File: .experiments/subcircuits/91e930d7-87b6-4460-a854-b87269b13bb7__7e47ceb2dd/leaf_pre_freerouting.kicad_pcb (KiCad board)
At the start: 2 copper layers, 34.9 x 18.6 mm, 13 parts, among them U2 BQ24072

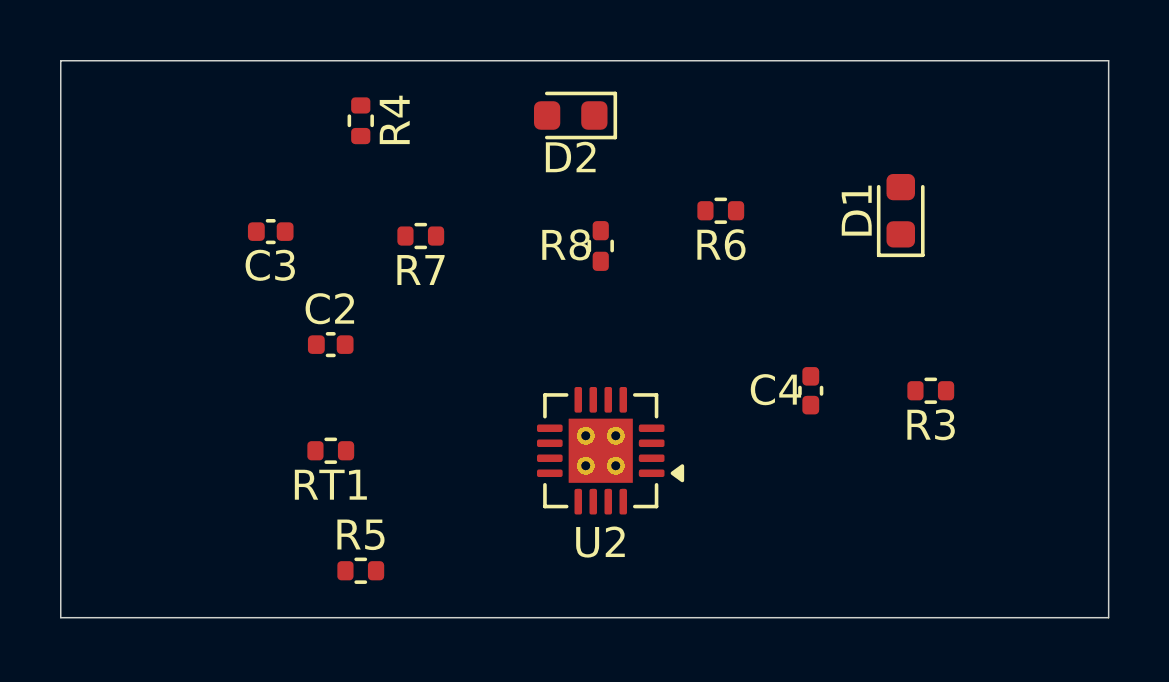
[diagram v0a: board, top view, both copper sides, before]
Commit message: feat: parent board stamping with preserved child copper
- Add --pcb, --stamp, --route, --jar flags to compose_subcircuits.py
- Implement subprocess-based parent board stamping (no pcbnew in main process)
- Add _stamp_parent_board() that copies base PCB, moves footprints to
  composed positions, clears existing tracks/zones, recreates child copper
  traces and vias with proper net name resolution
- Add _route_parent_board() for FreeRouting with preserve_existing_copper
- Add _persist_parent_artifact() for parent solved_layout.json persistence
- Store ParentComposition on ParentCompositionState for downstream access
- Update leaf artifacts from fresh pipeline run (6/6 leaves routed)
- Parent stamp verified: 37 components, 286 child traces, 10 vias preserved
  on real .kicad_pcb board with correct positions and net assignments
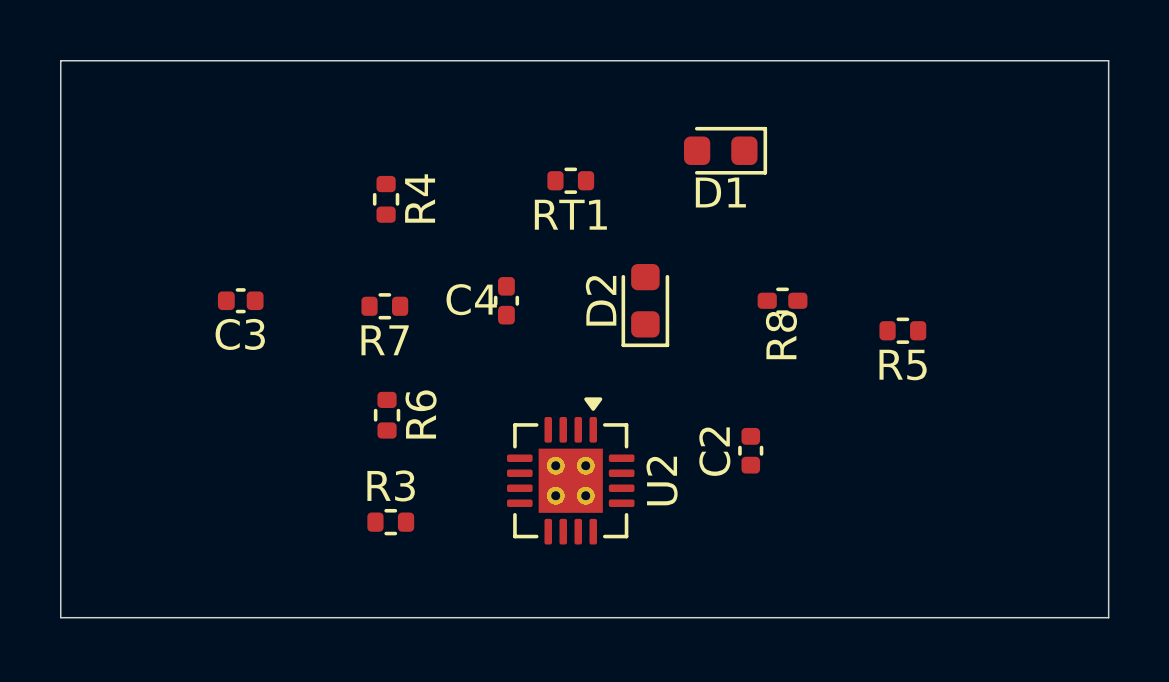
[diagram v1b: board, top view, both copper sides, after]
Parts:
- moved R5 19.8 mm to (28.1, 9.00), turned to 180 degrees
- moved R3 18.5 mm to (11.0, 15.4), turned to 0 degrees
- moved C2 14.4 mm to (23.0, 13.0), turned to 90 degrees
- moved R6 13.0 mm to (10.9, 11.8), turned to -90 degrees
- moved RT1 12.0 mm to (17.0, 4.00)
- moved C4 10.6 mm to (14.9, 8.00)
- moved D2 6.66 mm to (19.5, 8.00), turned to 90 degrees
- moved R8 6.33 mm to (24.1, 8.00), turned to 180 degrees
- moved D1 6.32 mm to (22.0, 3.00), turned to 180 degrees
- moved R4 2.75 mm to (10.8, 4.62)
- moved R7 2.63 mm to (10.8, 8.18)
- moved C3 2.51 mm to (6.00, 8.00)
- moved U2 1.41 mm to (17.0, 14.0), turned to -90 degrees

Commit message: feat: unified hierarchical solver (solve_hierarchy.py)
Single-command entry point for the full subcircuit pipeline:
  python3 solve_hierarchy.py LLUPS.kicad_sch --pcb LLUPS.kicad_pcb --route

Phase 1: Solve leaf subcircuits (delegates to solve_subcircuits.py)
  - 6 leaves solved and routed via FreeRouting
  - Canonical copper persisted in solved_layout.json

Phase 2: Compose and route parent (delegates to compose_subcircuits.py)
  - Grid layout of 6 children with 5mm spacing
  - Child copper preserved on stamped parent board
  - FreeRouting routes interconnect nets between subcircuits
  - Parent artifact persisted with full copper

Flags: --skip-leaves, --leaf-only, --rounds, --mode, --spacing-mm, --jar
Full pipeline completes in ~4 minutes (with routing)
Skip-leaves mode completes in ~28 seconds
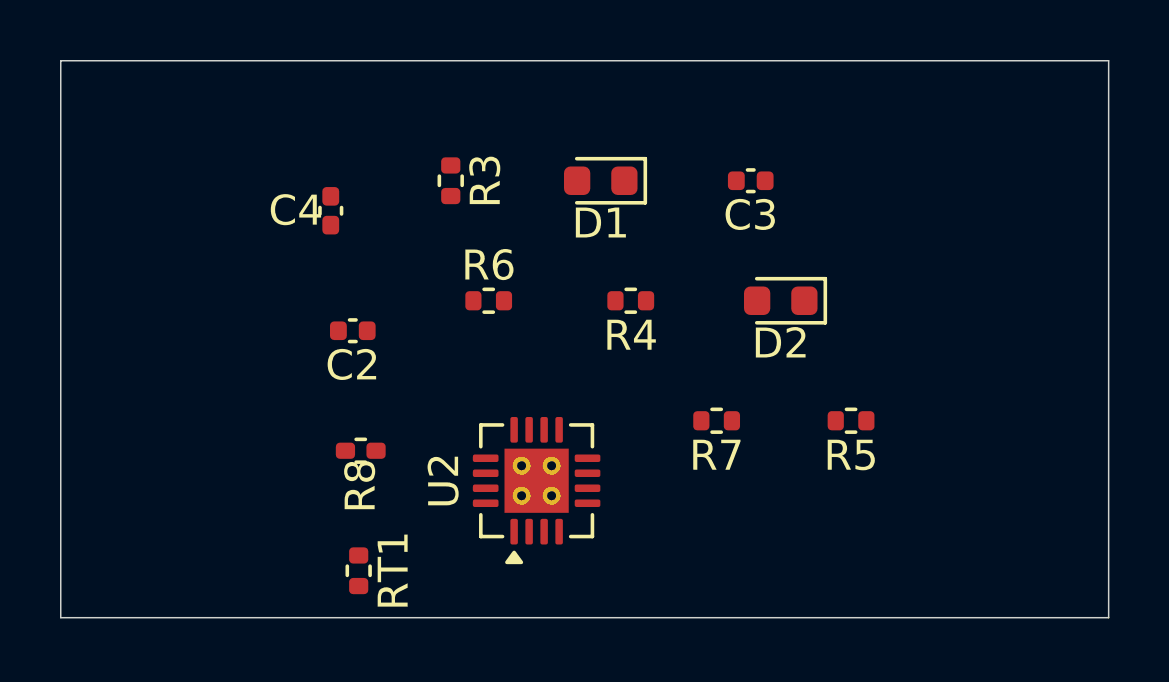
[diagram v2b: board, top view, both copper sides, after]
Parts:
- moved C3 17.5 mm to (23.0, 4.00)
- moved R8 14.9 mm to (10.0, 13.0)
- moved RT1 14.8 mm to (9.93, 17.0), turned to -90 degrees
- moved C2 13.9 mm to (9.73, 9.00), turned to 180 degrees
- moved R7 11.7 mm to (21.9, 12.0)
- moved R3 11.6 mm to (13.0, 4.00), turned to -90 degrees
- moved R4 8.83 mm to (19.0, 8.00), turned to 180 degrees
- moved C4 6.58 mm to (9.00, 5.00)
- moved R6 5.10 mm to (14.3, 8.00), turned to 0 degrees
- moved D2 4.51 mm to (24.0, 8.00), turned to 180 degrees
- moved D1 4.12 mm to (18.0, 4.00)
- moved R5 3.46 mm to (26.3, 12.0)
- moved U2 1.14 mm to (15.9, 14.0), turned to 90 degrees
